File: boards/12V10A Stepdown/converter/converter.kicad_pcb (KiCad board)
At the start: 4 copper layers, 27 parts, among them J1 TB005-762-02BE, J2 TB005-762-02BE, M1 CSD17578Q3A, M2 CSD17571Q2, U1 LM25145RGYR

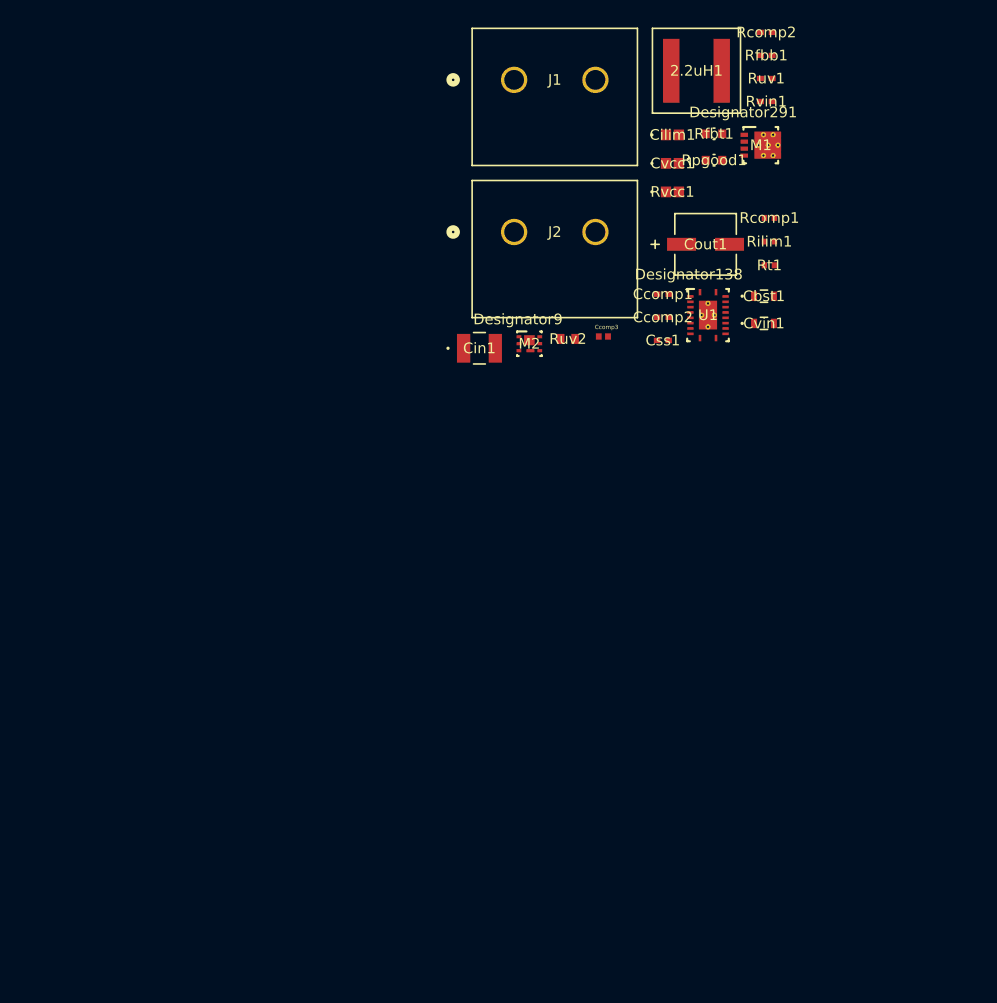
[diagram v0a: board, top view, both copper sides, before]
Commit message: iris silkscreen stuff for 20a board
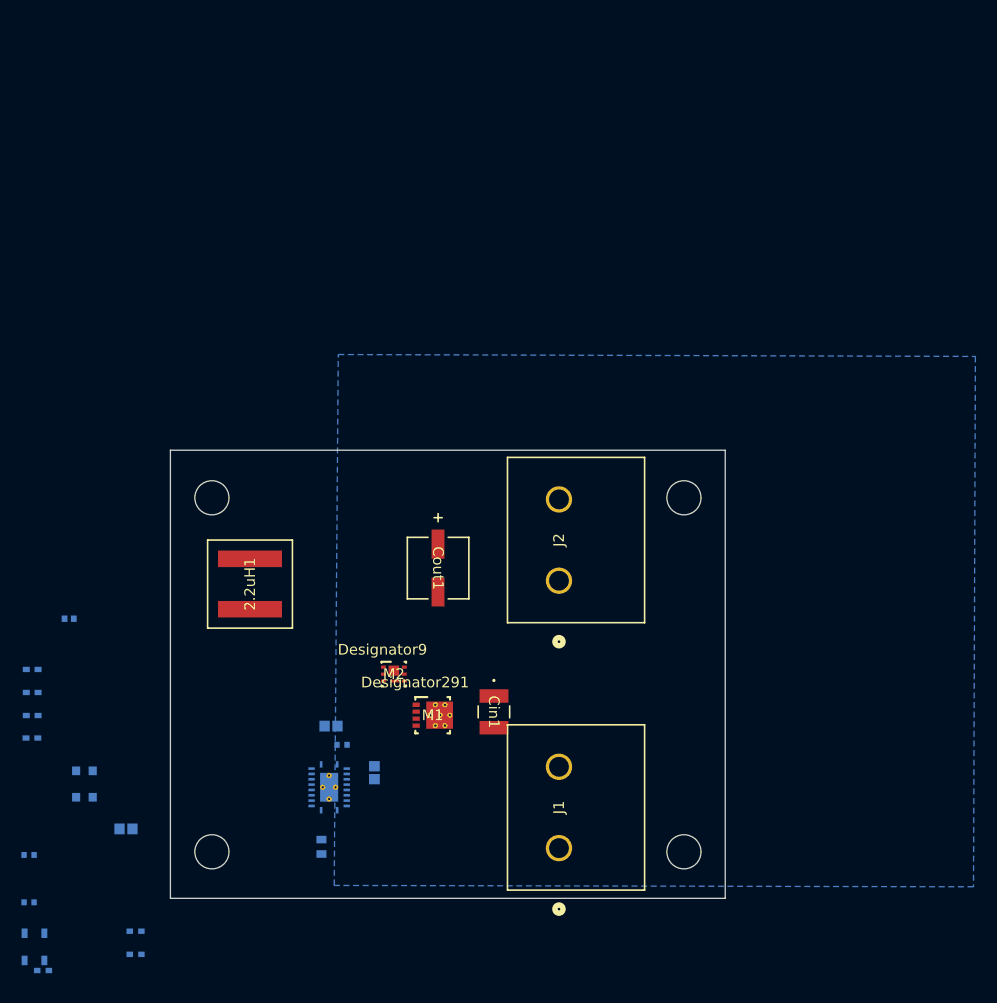
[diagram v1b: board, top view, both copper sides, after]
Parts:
- added REF**: MountingHole_3.2mm_M3, MountingHole:MountingHole_3.2mm_M3, F.Cu at (101.9, 137.6)
- added REF**: MountingHole_3.2mm_M3, MountingHole:MountingHole_3.2mm_M3, F.Cu at (101.9, 104.5)
- added REF**: MountingHole_3.2mm_M3, MountingHole:MountingHole_3.2mm_M3, F.Cu at (146.1, 137.6)
- added REF**: MountingHole_3.2mm_M3, MountingHole:MountingHole_3.2mm_M3, F.Cu at (146.1, 104.5)
- Cbst1, Ccomp1, Ccomp2, Ccomp3, Cilim1, Css1, Cvcc1, Cvin1, Rcomp1, Rcomp2, Rfbb1, Rfbt1, Rilim1, Rpgood1, Rt1, Ruv1, Ruv2, Rvcc1, Rvin1, U1: moved to B.Cu
- moved Rcomp1 91.5 mm to (84.8, 137.9), turned to 180 degrees
- moved Rt1 91.5 mm to (84.8, 142.4), turned to 180 degrees
- moved Rfbb1 91.1 mm to (85.0, 122.7), turned to 180 degrees
- moved Ruv1 91.1 mm to (85.0, 124.9), turned to 180 degrees
- moved Rcomp2 91.1 mm to (85.0, 120.5), turned to 180 degrees
- moved Rvin1 91.1 mm to (85.0, 127.0), turned to 180 degrees
- moved Cbst1 90.8 mm to (85.3, 145.3), turned to 180 degrees
- moved Cvin1 90.8 mm to (85.3, 147.8), turned to 180 degrees
- moved Rfbt1 83.9 mm to (89.9, 130.1), turned to 180 degrees
- moved Rpgood1 83.9 mm to (89.9, 132.5), turned to 180 degrees
- moved Css1 82.8 mm to (86.1, 148.8), turned to 180 degrees
- moved Rvcc1 78.7 mm to (93.8, 135.5), turned to 180 degrees
- moved Ccomp1 77.5 mm to (94.7, 145.1), turned to 180 degrees
- moved Ccomp2 77.5 mm to (94.7, 147.2), turned to 180 degrees
- moved J1 72.1 mm to (134.4, 137.3), turned to 90 degrees
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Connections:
- net Net-(2.2uH1-Pad2) renamed /Vout
- Cin1 pad 1: Net-(M1-D5) -> /Vin
- J1 pad 1: GND -> /Vin
- J1 pad 2: Net-(M1-D5) -> GND
- M1 pad 5: Net-(M1-D5) -> /Vin
- Ruv1 pad 1: Net-(M1-D5) -> /Vin
- Rvin1 pad 1: Net-(M1-D5) -> /Vin
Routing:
- added copper zone on B.Cu, net GND
- added copper zone on In1.Cu, net GND
- added copper zone on In2.Cu, net GND
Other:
- board outline added: 52 x 42 mm

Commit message: moved en/vulo trace to higher gnd layer
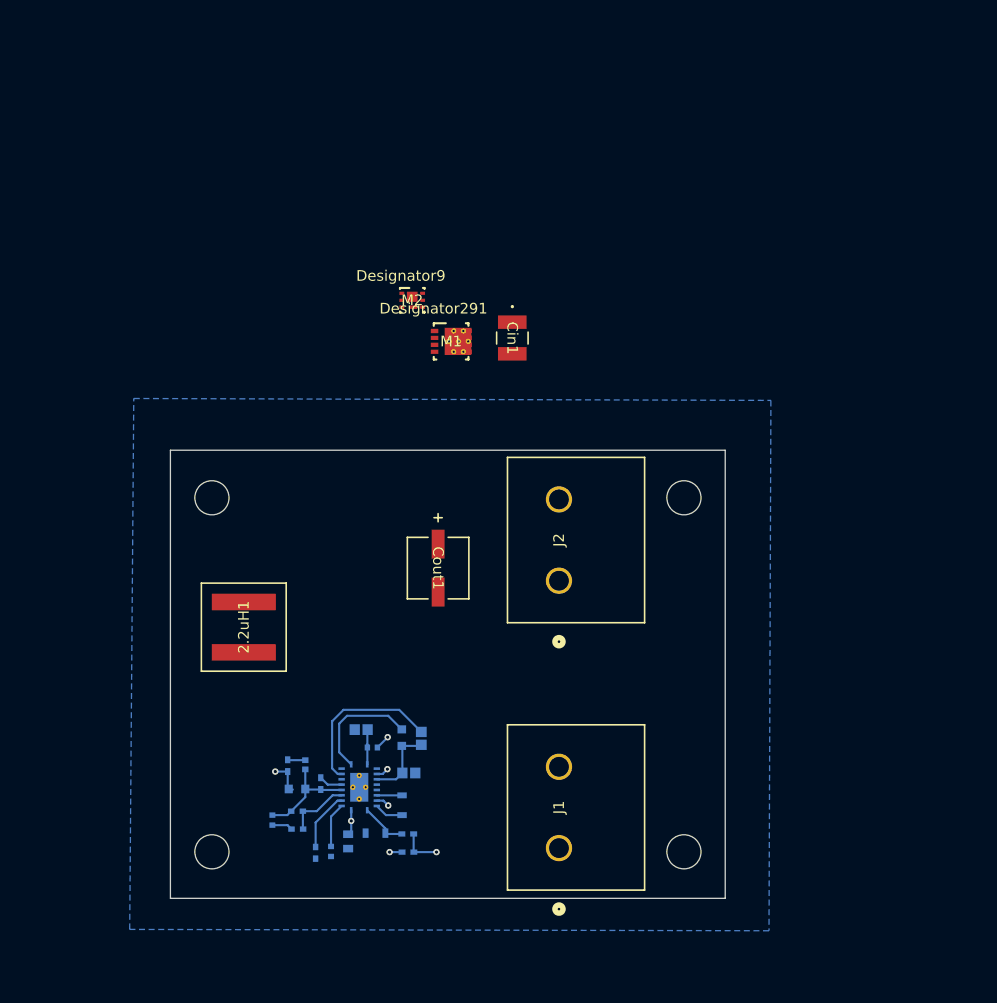
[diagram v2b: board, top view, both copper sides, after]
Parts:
- moved Ruv1 37.5 mm to (120.3, 137.7)
- moved Cbst1 36.5 mm to (119.7, 133.3), turned to -90 degrees
- moved Rvin1 36.4 mm to (120.2, 136.0)
- moved M1 35.1 mm to (124.3, 89.8)
- moved Cin1 35.1 mm to (130.0, 89.5)
- moved M2 35.1 mm to (120.7, 85.9)
- moved Cvin1 34.1 mm to (117.2, 135.9)
- moved Rpgood1 30.3 mm to (119.7, 126.9), turned to -90 degrees
- moved Rvcc1 28.9 mm to (121.5, 127.0), turned to -90 degrees
- moved Rt1 28.7 mm to (113.1, 137.6), turned to -90 degrees
- moved Rfbb1 28.4 mm to (112.1, 131.2), turned to 90 degrees
- moved Css1 27.8 mm to (111.6, 137.7), turned to -90 degrees
- moved Ccomp3 26.0 mm to (110.6, 129.5), turned to -90 degrees
- moved Rcomp2 25.6 mm to (109.0, 129.6), turned to 90 degrees
- moved Rcomp1 23.0 mm to (107.6, 134.7), turned to 90 degrees
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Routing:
- net Net-(U1-SYNCIN): track 0.00 -> 15.2 mm
- net Net-(U1-PGOOD): track 0.00 -> 11.0 mm
- net Net-(U1-FB): track 0.00 -> 9.82 mm
- net Net-(U1-VCC): track 0.00 -> 7.07 mm
- net Net-(U1-COMP): track 0.00 -> 5.94 mm
- net Net-(U1-SS/TRK): track 0.00 -> 5.58 mm
- net Net-(U1-VIN): track 0.00 -> 4.43 mm
- net Net-(U1-RT): track 0.00 -> 4.20 mm
- net Net-(M1-S1): track 0.00 -> 4.08 mm, vias 0 -> 1
- net /Vin: track 0.00 -> 4.02 mm, vias 0 -> 1
- net Net-(U1-EN/UVLO): track 0.00 -> 3.76 mm, vias 0 -> 2
- net Net-(U1-ILIM): track 0.00 -> 3.32 mm
- net /Vout: track 0.00 -> 2.88 mm, vias 0 -> 1
- net Net-(U1-BST): track 0.00 -> 2.37 mm
- net GND: track 0.00 -> 2.22 mm
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
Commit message: minor fixes
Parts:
- moved Cin1 38.7 mm to (127.3, 128.1), turned to 90 degrees
- moved M2 36.7 mm to (120.7, 122.7)
- moved M1 33.8 mm to (124.3, 123.6)
- moved Cout1 4.57 mm to (121.2, 106.9)
- moved 2.2uH1 1.75 mm to (104.2, 115.0)
- moved Rpgood1 1.51 mm to (118.8, 128.1)
- moved Cvin1 1.49 mm to (116.3, 137.0)
- moved Rvin1 1.47 mm to (119.3, 137.1)
- moved Ruv2 1.43 mm to (113.5, 137.6)
- moved Rvcc1 1.42 mm to (120.6, 128.1)
- moved Cbst1 1.28 mm to (118.8, 134.2)
- moved Cilim1 1.28 mm to (115.0, 127.1)
- moved Cvcc1 1.28 mm to (119.4, 131.1)
- moved Rcomp2 1.28 mm to (108.1, 130.5)
- moved Rfbb1 1.28 mm to (111.2, 132.1)
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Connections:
- U1 pad V: (no net) -> GND
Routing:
- net Net-(U1-EN/UVLO): track 3.76 -> 9.87 mm
- net GND: track 2.22 -> 4.53 mm, vias 0 -> 1
- net /Vin: track 4.02 -> 2.34 mm
- net Net-(U1-VCC): track 7.07 -> 5.43 mm
- net Net-(U1-VIN): track 4.43 -> 2.96 mm
- net Net-(U1-SS/TRK): track 5.58 -> 4.44 mm
- net Net-(U1-RT): track 4.20 -> 3.12 mm

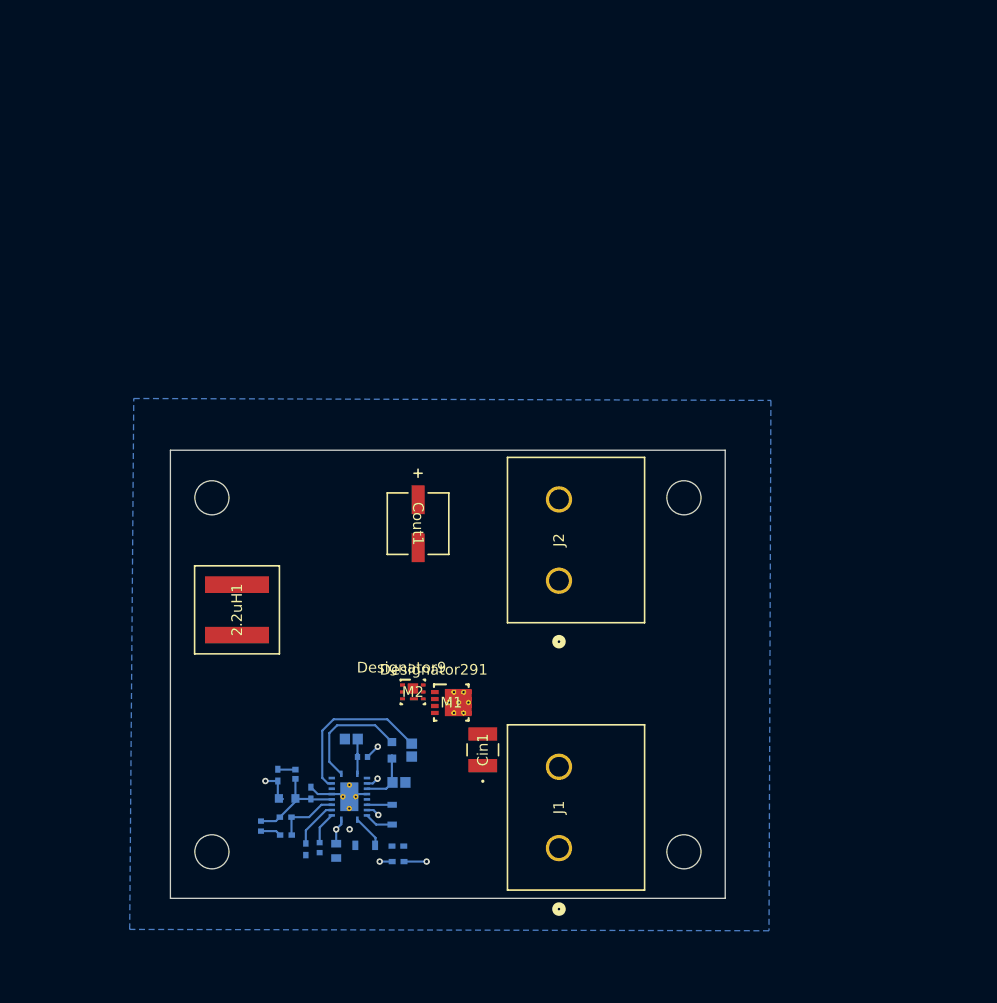
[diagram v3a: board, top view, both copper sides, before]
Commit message: 10a stepdown and 20a stepdown update
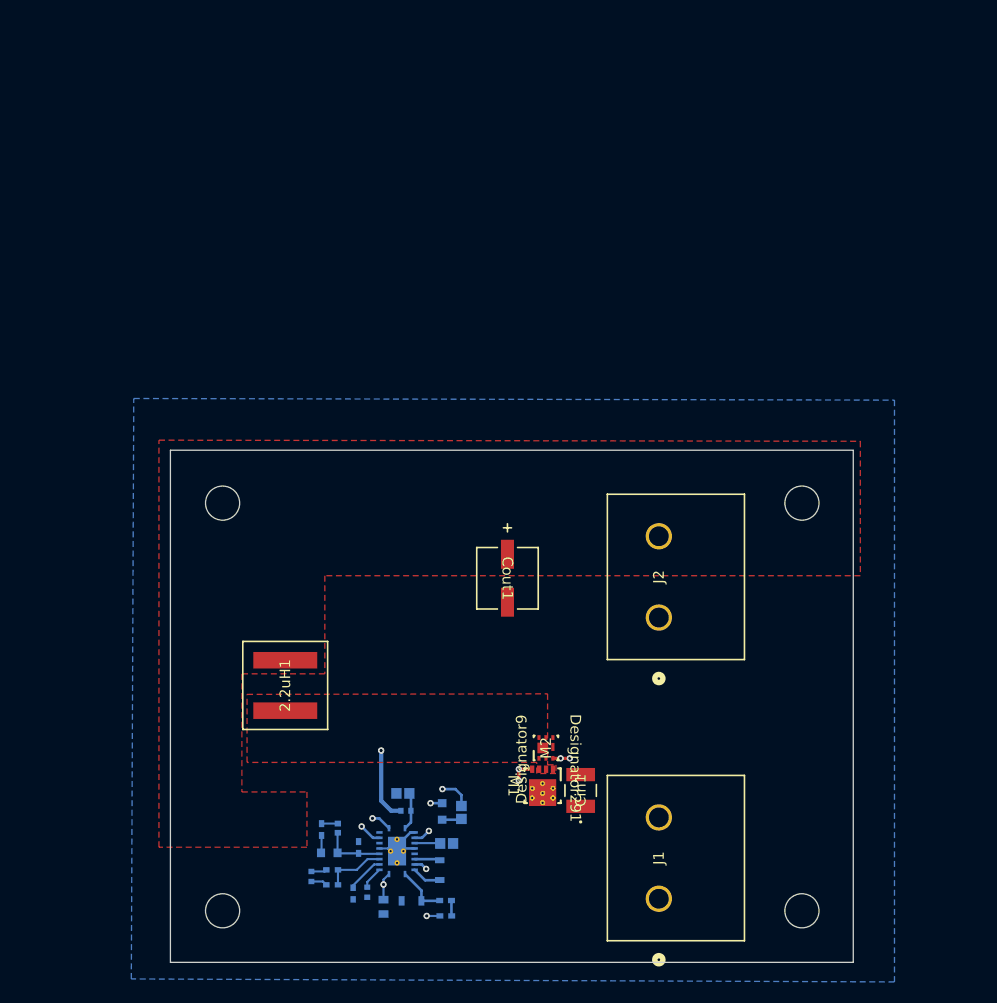
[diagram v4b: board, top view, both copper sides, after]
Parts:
- moved M2 13.5 mm to (133.2, 127.9), turned to 90 degrees
- moved REF** 12.4 mm to (157.2, 143.2)
- moved M1 11.6 mm to (132.9, 131.4), turned to -90 degrees
- moved REF** 11.1 mm to (157.2, 105.0)
- moved J1 10.5 mm to (143.8, 142.0)
- moved J2 9.98 mm to (143.8, 115.7)
- moved Cin1 9.93 mm to (136.4, 131.9)
- moved Cout1 9.82 mm to (129.6, 112.0)
- moved 2.2uH1 8.41 mm to (108.8, 122.0)
- moved Rvcc1 7.47 mm to (125.3, 134.0)
- moved Rpgood1 7.42 mm to (123.5, 133.9)
- moved Cvcc1 7.26 mm to (123.9, 136.9)
- moved Cilim1 7.02 mm to (119.8, 132.2)
- moved Ruv2 6.87 mm to (118.0, 142.8)
- moved Cbst1 6.85 mm to (123.2, 139.4)
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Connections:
- M1 pad 2: unconnected-(M1-S2-Pad2) -> Net-(M1-S1)
- M1 pad 3: unconnected-(M1-S3-Pad3) -> Net-(M1-S1)
- M1 pad 6: unconnected-(M1-D6-Pad6) -> /Vin
- M1 pad 7: unconnected-(M1-D7-Pad7) -> /Vin
- M1 pad 8: unconnected-(M1-D8-Pad8) -> /Vin
- M1 pad 9: (no net) -> /Vin
- M1 pad V: (no net) -> /Vin
- M2 pad 7: Net-(M1-S1) -> GND
- M2 pad 8: GND -> Net-(M1-S1)
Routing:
- net Net-(U1-LO): track 1.18 -> 26.1 mm, vias 1 -> 3
- net Net-(M1-G): track 1.26 -> 18.2 mm, vias 1 -> 3
- net Net-(M1-S1): track 4.08 -> 9.75 mm
- net Net-(U1-FB): track 9.56 -> 7.48 mm
- net Net-(U1-SYNCIN): track 15.3 -> 17.3 mm, vias 0 -> 2
- net Net-(U1-VIN): track 2.96 -> 4.86 mm
- net Net-(U1-PGOOD): track 11.1 -> 12.8 mm, vias 0 -> 2
- net /Vout: track 2.88 -> 1.65 mm, vias 1 -> 0
- net GND: track 4.53 -> 5.57 mm, vias 1 -> 0
- net Net-(U1-VCC): track 5.43 -> 4.41 mm
- net Net-(U1-RT): track 3.12 -> 2.10 mm
- net Net-(U1-SS/TRK): track 4.44 -> 3.50 mm
- net /Vin: track 2.34 -> 1.46 mm, vias 1 -> 0
- added copper zone on F.Cu, net /Vout
- added copper zone on F.Cu, net Net-(M1-S1)
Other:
- board size 52 x 42 mm -> 64 x 48 mm

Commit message: moved 20a terminal vias and some 10a stuff
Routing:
- net Net-(M1-S1): track 9.75 -> 24.1 mm, vias 1 -> 2
- net /Vout: track 1.65 -> 3.99 mm, vias 0 -> 40
- net /Vin: track 1.46 -> 3.77 mm, vias 0 -> 28
- net GND: vias 0 -> 67
- added copper zone on F.Cu, net /Vin
- added copper zone on F.Cu, net GND
